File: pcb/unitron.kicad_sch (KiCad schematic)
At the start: 67 parts, among them J1 Conn_01x09_Female, J2 Conn_01x09_Male, J3 Conn_01x09_Female, J4 Conn_01x09_Male, J5 Conn_02x03_Odd_Even, Q1 FDN340P, Q2 BSS123, SW1 SW_SPST, U1 LTC-4727JS, U2 LTC-4727JS, U3 AS1115-BSST, U4 ATSAMD21E, U5 LTC-4727JR, U6 LTC-4727JR, U7 AS1115-BSST

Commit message: PCB v1.5
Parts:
- removed BT2: 2466, Battery:BatteryHolder_Keystone_2466_1xAAA, symbol Device:Battery
- removed D14: LED, LED_SMD:LED_0805_2012Metric, symbol Device:LED
- removed R2: 10KΩ, Resistor_SMD:R_0805_2012Metric, symbol Device:R_Small_US
- added S16: Gateron Blue, Button_Switch_Keyboard:SW_Cherry_MX_1.00u_PCB, symbol imperializer-rescue:switch_momentary_2pin-asl_symbols-imperializer-rescue
- added U8: AT24C01C-STUM, Package_TO_SOT_SMD:SOT-23-5, symbol asl_symbols_new:AT24C01C-STUM
- BT1: value 2466 -> 2468
- D1, D10, D11, D12, D2, D3, D4, D5, D6, D7, D8, D9: footprint LED_SMD:LED-APA102-2020 -> asl_footprints:LED-APA102-2020
- J1, J3: footprint Connector_PinSocket_2.54mm:PinSocket_1x09_P2.54mm_Vertical -> Connector_PinSocket_2.54mm:PinSocket_1x09_P2.54mm_Vertical_SMD_Pin1Left
- S4: footprint Button_Switch_Keyboard:SW_Cherry_MX_2.00u_PCB -> Button_Switch_Keyboard:SW_Cherry_MX_1.00u_PCB
- SW1: footprint asl_footprints:B12AP -> asl_footprints:switch_nkk_reinforced_pc_pin
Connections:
- net CKI: now also D6.4 (SDI), J3.8 (Pin_8); no longer D12.5 (CKI), J3.1 (Pin_1)
- net GND: now also BT1.2 (-), C2.2, J4.1 (Pin_1), U8.2 (GND), U8.5 (WP); no longer J4.3 (Pin_3)
- net GND_daughter: now also J3.1 (Pin_1); no longer J3.3 (Pin_3)
- net IRQ: now also J3.7 (Pin_7); no longer J3.9 (Pin_9)
- net IRQ_mcu: now also J4.7 (Pin_7); no longer J4.9 (Pin_9)
- net KEYA: now also J4.5 (Pin_5), S16.1; no longer J4.7 (Pin_7)
- net KEYB: now also J4.6 (Pin_6); no longer J4.8 (Pin_8)
- net MOSI: now also J4.9 (Pin_9); no longer J4.2 (Pin_2)
- net SCK: now also J4.8 (Pin_8); no longer J4.1 (Pin_1)
- net SCL: now also J3.3 (Pin_3); no longer J3.5 (Pin_5)
- net SCL_mcu: now also J4.3 (Pin_3), U8.1 (SCL); no longer J4.5 (Pin_5)
- net SDA: now also J3.4 (Pin_4); no longer J3.6 (Pin_6)
- net SDA_mcu: now also J4.4 (Pin_4), U8.3 (SDA); no longer J4.6 (Pin_6)
- net SDI: now also D6.5 (CKI), J3.9 (Pin_9); no longer D12.4 (SDI), J3.2 (Pin_2)
- net VIN: now also J4.2 (Pin_2), U8.4 (Vcc); no longer J4.4 (Pin_4)
- net VIN_daughter: now also J3.2 (Pin_2); no longer J3.4 (Pin_4)
- net at U3.11 (KEYA): now also J3.5 (Pin_5); no longer J3.7 (Pin_7)
- net at U3.12 (KEYB): now also J3.6 (Pin_6); no longer J3.8 (Pin_8)
- net at J2.7 (Pin_7), S12.2: now also S16.2
- net at D8.2 (CKO): now also D1.5 (CKI); no longer D2.5 (CKI)
- net at D8.3 (SDO): now also D1.4 (SDI); no longer D2.4 (SDI)
- net at D8.4 (SDI): now also D2.3 (SDO); no longer D3.3 (SDO)
- net at D8.5 (CKI): now also D2.2 (CKO); no longer D3.2 (CKO)
- net at D3.4 (SDI): now also D10.3 (SDO); no longer D9.3 (SDO)
- net at D3.5 (CKI): now also D10.2 (CKO); no longer D9.2 (CKO)
- net at D1.2 (CKO): now also D7.5 (CKI)
- net at D1.3 (SDO): now also D7.4 (SDI)
- net at D7.3 (SDO): no longer D1.4 (SDI)
- net at D7.2 (CKO): no longer D1.5 (CKI)
- net at D12.2 (CKO): now also D5.5 (CKI); no longer D6.5 (CKI)
- net at D12.3 (SDO): now also D5.4 (SDI); no longer D6.4 (SDI)
- net at D9.4 (SDI): now also D3.3 (SDO); no longer D4.3 (SDO)
- net at D9.5 (CKI): now also D3.2 (CKO); no longer D4.2 (CKO)
- net at D5.2 (CKO): now also D11.5 (CKI); no longer D10.5 (CKI)
- net at D5.3 (SDO): now also D11.4 (SDI); no longer D10.4 (SDI)
- net at D11.3 (SDO): now also D4.4 (SDI); no longer D5.4 (SDI)
- net at D11.2 (CKO): now also D4.5 (CKI); no longer D5.5 (CKI)
- net at D6.2 (CKO): now also D12.5 (CKI); no longer D11.5 (CKI)
- net at D6.3 (SDO): now also D12.4 (SDI); no longer D11.4 (SDI)
- net neopixel_mcu: no longer names the net of U4.11 (PA08(D4))
- new net: D2.4 (SDI), D9.3 (SDO)
- new net: D2.5 (CKI), D9.2 (CKO)
- new net: D10.5 (CKI), D4.2 (CKO)
- new net: D10.4 (SDI), D4.3 (SDO)
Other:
- moved on the sheet: BT1, D1, D10, D11, D12, D2, D3, D4, D5, D6, D7, D8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

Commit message: pcb v1.6
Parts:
- removed D1, D10, D11, D12, D2, D3, D4, D5, D6, D7, D8, D9: APA102-2020, asl_footprints:LED-APA102-2020, symbol LED:APA102-2020
- added D1, D10, D2, D3, D4, D5, D6, D7, D8, D9: SK9822, asl_footprints:LED_SK9822_5050, symbol asl_symbols_new:SK9822
- added R7, R8: 10KΩ, Resistor_SMD:R_0805_2012Metric, symbol Device:R_Small_US
- added U1: AP2112K-3.3, Package_TO_SOT_SMD:SOT-23-5, symbol asl_symbols_new:AP2112K-3.3
- BT1: footprint Battery:BatteryHolder_Keystone_2468_2xAAA -> Battery:BatteryHolder_Keystone_2479_3xAAA
- C2, C3: value 0.1µF -> 100nF
- J1, J3: value Conn_01x09_Female -> Conn_01x10_Male; footprint Connector_PinSocket_2.54mm:PinSocket_1x09_P2.54mm_Vertical_SMD_Pin1Left -> Connector_PinSocket_2.54mm:PinSocket_1x10_P2.54mm_Vertical_SMD_Pin1Right; symbol Connector:Conn_01x09_Female -> Connector:Conn_01x10_Male
- J2, J4: value Conn_01x09_Male -> Conn_01x10_Female; footprint Connector_PinHeader_2.54mm:PinHeader_1x09_P2.54mm_Vertical -> Connector_PinHeader_2.54mm:PinHeader_1x10_P2.54mm_Vertical; symbol Connector:Conn_01x09_Male -> Connector:Conn_01x10_Female
- renumbered D13 to D11, R9 to R10, R10 to R11, R11 to R12, R12 to R13, R13 to R14, R14 to R15, R3 to R2, R4 to R3, R5 to R4, R6 to R5, R7 to R6, R8 to R9, S9 to S10, S10 to S11, S11 to S12, S12 to S13, S13 to S14, S14 to S15, S15 to S16, S16 to S7, S7 to S8, S8 to S9, U1 to U2, U2 to U3, U3 to U4, U4 to U5, U8 to U6, U5 to U7, U6 to U8, U7 to U9
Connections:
- net CKI: now also D5.2 (CI)
- net GND: now also R8.2, U1.2 (GND)
- net GND_daughter: now also D1.3 (GND), D10.3 (GND), D2.3 (GND), D3.3 (GND), D4.3 (GND), D5.3 (GND), D6.3 (GND), D7.3 (GND), D8.3 (GND), D9.3 (GND)
- net SDI: now also D5.1 (DI)
- net VBATT: now also R7.1
- net VIN: now also U1.5 (VOUT); no longer Q1.3 (D)
- net VIN_daughter: now also D1.4 (VCC), D10.4 (VCC), D2.4 (VCC), D3.4 (VCC), D4.4 (VCC), D5.4 (VCC), D6.4 (VCC), D7.4 (VCC), D8.4 (VCC), D9.4 (VCC)
- net at J2.7 (Pin_7), S13.2: no longer S7.2
- net at J2.9 (Pin_9), S15.2: now also S7.2
- net batt_lvl: now reaches U5.6 (PA05(A4))
- net batt_lvl: now also R7.2, R8.1
- new net: Q1.3 (D), U1.1 (VIN), U1.3 (EN)
- new net: D10.6 (DO), D4.1 (DI)
- new net: D10.5 (CO), D4.2 (CI)
- new net: D4.5 (CO), D9.2 (CI)
- new net: D4.6 (DO), D9.1 (DI)
- new net: D2.6 (DO), D7.1 (DI)
- new net: D2.5 (CO), D7.2 (CI)
- new net: D1.2 (CI), D7.5 (CO)
- new net: D1.1 (DI), D7.6 (DO)
- new net: D1.6 (DO), D6.1 (DI)
- new net: D1.5 (CO), D6.2 (CI)
- new net: D3.1 (DI), D9.6 (DO)
- new net: D3.2 (CI), D9.5 (CO)
- new net: D3.5 (CO), D8.2 (CI)
- new net: D3.6 (DO), D8.1 (DI)
- new net: D2.2 (CI), D8.5 (CO)
- new net: D2.1 (DI), D8.6 (DO)
- new net: D10.2 (CI), D5.5 (CO)
- new net: D10.1 (DI), D5.6 (DO)
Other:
- moved on the sheet: BT1, C1, C2, C3, D11, H1, H2, H3, H4, J5, Q1, Q2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

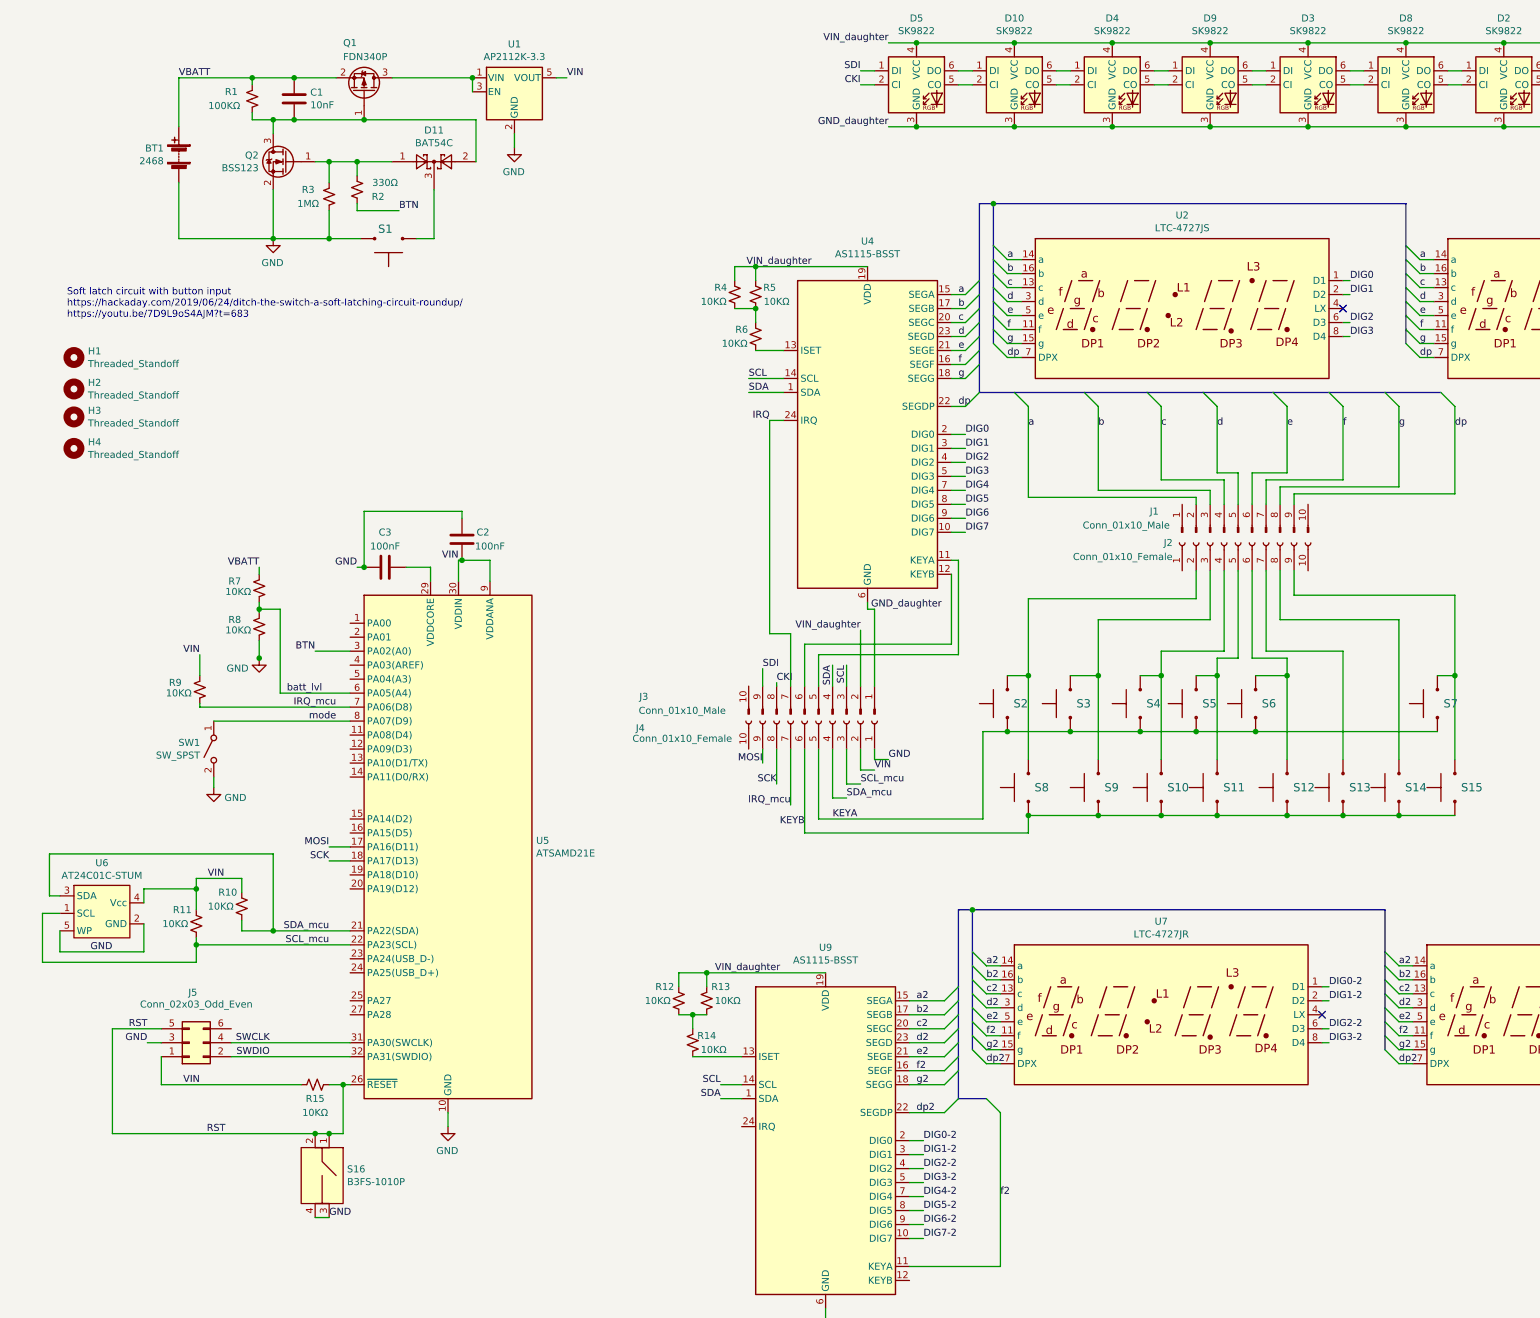
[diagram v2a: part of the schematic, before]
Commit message: unitron v 1.8
changed to QT PY and added lipo battery charging circuit
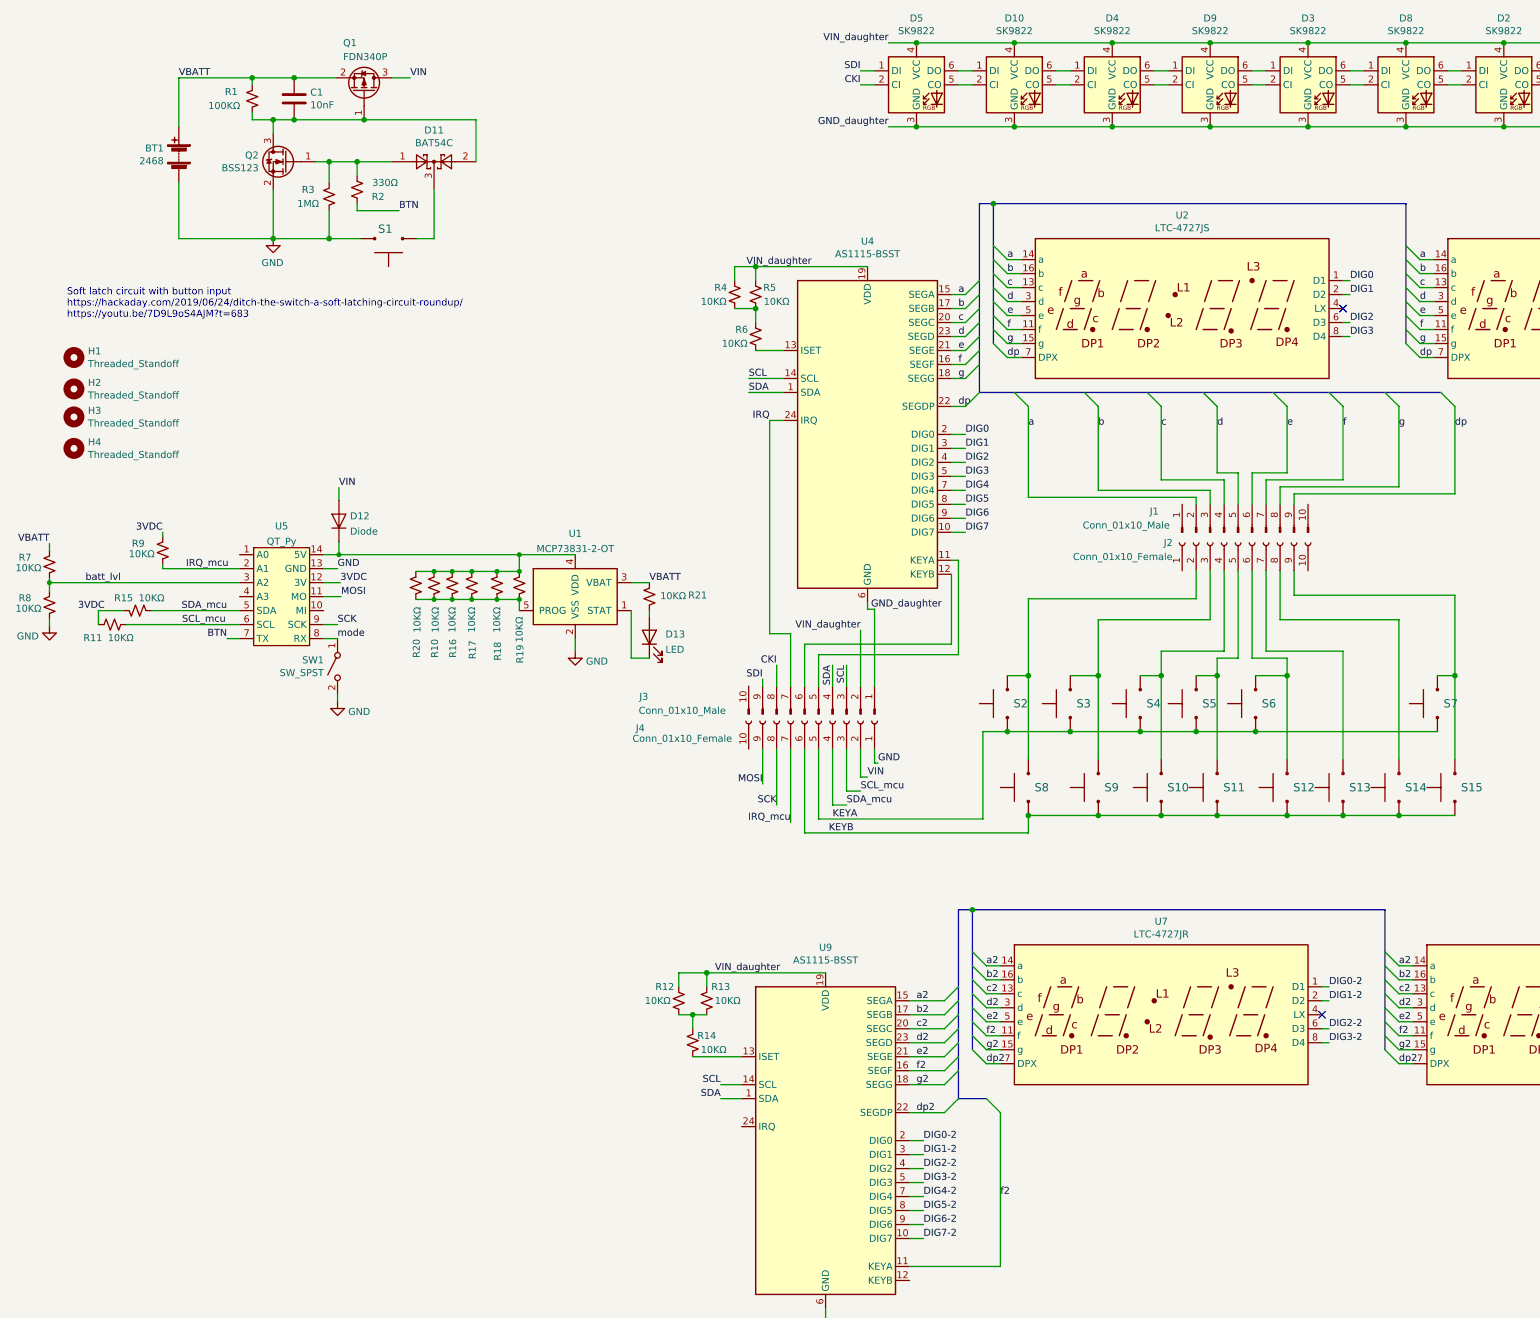
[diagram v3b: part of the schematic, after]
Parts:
- removed C2, C3: 100nF, Capacitor_SMD:C_0805_2012Metric, symbol Device:C
- removed J5: Conn_02x03_Odd_Even, asl_footprints:Tag-Connect_TC2030-IDC-NL_2x03_P1.27mm_Vertical, symbol Connector_Generic:Conn_02x03_Odd_Even
- removed S16: B3FS-1010P, asl_footprints:6mm_tactile_smd, symbol asl_symbols:B3FS-1010P
- removed U1: AP2112K-3.3, Package_TO_SOT_SMD:SOT-23-5, symbol asl_symbols_new:AP2112K-3.3
- removed U5: ATSAMD21E, Package_QFP:TQFP-32_7x7mm_P0.8mm, symbol asl_symbols_new:ATSAMD21E
- removed U6: AT24C01C-STUM, Package_TO_SOT_SMD:SOT-23-5, symbol asl_symbols_new:AT24C01C-STUM
- added D12: Diode, asl_footprints:D_SOD-123F, symbol asl_symbols_new:Diode
- added D13: LED, LED_SMD:LED_0805_2012Metric, symbol Device:LED
- added R16, R17, R18, R19, R20, R21: 10KΩ, Resistor_SMD:R_0805_2012Metric, symbol Device:R_Small_US
- added U1: MCP73831-2-OT, Package_TO_SOT_SMD:SOT-23-5, symbol Battery_Management:MCP73831-2-OT
- added U5: QT_Py, asl_footprints:QT_Py, symbol asl_symbols_new:QT_Py
- BT1: footprint Battery:BatteryHolder_Keystone_2479_3xAAA -> Connector_PinHeader_2.54mm:PinHeader_1x02_P2.54mm_Vertical
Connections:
- net RST is gone; now on net SDA_mcu: R15.1
- net BTN: now also U5.7 (TX)
- net GND: now also U1.2 (VSS), U5.13 (GND)
- net IRQ_mcu: now also U5.2 (A1)
- net MOSI: now also U5.11 (MO)
- net SCK: now also U5.9 (SCK)
- net SCL_mcu: now also U5.6 (SCL)
- net SDA_mcu: now also U5.5 (SDA); no longer R10.1
- net VBATT: now also R21.1, U1.3 (VBAT)
- net VIN: now also Q1.3 (D), D12.2 (A); no longer R10.2, R11.2, R15.2, R9.1
- net batt_lvl: now also U5.3 (A2)
- net mode: now also U5.8 (RX)
- new net: D12.1 (K), R10.1, R16.1, R17.1, R18.1, R19.1, R20.1, U1.4 (VDD), U5.14 (5V)
- new net: R10.2, R16.2, R17.2, R18.2, R19.2, R20.2, U1.5 (PROG)
- new net: D13.2 (A), R21.2
- new net: D13.1 (K), U1.1 (STAT)
- new net 3VDC: R11.2, R15.2, R9.1, U5.12 (3V)

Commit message: pcb v1.9
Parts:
- removed R10, R16, R17, R18, R20: 10KΩ, Resistor_SMD:R_0805_2012Metric, symbol Device:R_Small_US
- added R7, R8: 10KΩ, Resistor_SMD:R_0805_2012Metric, symbol Device:R_Small_US
- D1: renamed from D5; value SK9822 -> WS2812B; footprint asl_footprints:LED_SK9822_5050 -> LED_SMD:LED_WS2812B_PLCC4_5.0x5.0mm_P3.2mm; symbol asl_symbols_new:SK9822 -> LED:WS2812B
- D10: renamed from D6; value SK9822 -> WS2812B; footprint asl_footprints:LED_SK9822_5050 -> LED_SMD:LED_WS2812B_PLCC4_5.0x5.0mm_P3.2mm; symbol asl_symbols_new:SK9822 -> LED:WS2812B
- D2: renamed from D10; value SK9822 -> WS2812B; footprint asl_footprints:LED_SK9822_5050 -> LED_SMD:LED_WS2812B_PLCC4_5.0x5.0mm_P3.2mm; symbol asl_symbols_new:SK9822 -> LED:WS2812B
- D3: renamed from D4; value SK9822 -> WS2812B; footprint asl_footprints:LED_SK9822_5050 -> LED_SMD:LED_WS2812B_PLCC4_5.0x5.0mm_P3.2mm; symbol asl_symbols_new:SK9822 -> LED:WS2812B
- D4: renamed from D9; value SK9822 -> WS2812B; footprint asl_footprints:LED_SK9822_5050 -> LED_SMD:LED_WS2812B_PLCC4_5.0x5.0mm_P3.2mm; symbol asl_symbols_new:SK9822 -> LED:WS2812B
- D5: renamed from D3; value SK9822 -> WS2812B; footprint asl_footprints:LED_SK9822_5050 -> LED_SMD:LED_WS2812B_PLCC4_5.0x5.0mm_P3.2mm; symbol asl_symbols_new:SK9822 -> LED:WS2812B
- D6: renamed from D8; value SK9822 -> WS2812B; footprint asl_footprints:LED_SK9822_5050 -> LED_SMD:LED_WS2812B_PLCC4_5.0x5.0mm_P3.2mm; symbol asl_symbols_new:SK9822 -> LED:WS2812B
- D7: renamed from D2; value SK9822 -> WS2812B; footprint asl_footprints:LED_SK9822_5050 -> LED_SMD:LED_WS2812B_PLCC4_5.0x5.0mm_P3.2mm; symbol asl_symbols_new:SK9822 -> LED:WS2812B
- D8: renamed from D7; value SK9822 -> WS2812B; footprint asl_footprints:LED_SK9822_5050 -> LED_SMD:LED_WS2812B_PLCC4_5.0x5.0mm_P3.2mm; symbol asl_symbols_new:SK9822 -> LED:WS2812B
- D9: renamed from D1; value SK9822 -> WS2812B; footprint asl_footprints:LED_SK9822_5050 -> LED_SMD:LED_WS2812B_PLCC4_5.0x5.0mm_P3.2mm; symbol asl_symbols_new:SK9822 -> LED:WS2812B
- J1, J3: footprint Connector_PinSocket_2.54mm:PinSocket_1x10_P2.54mm_Vertical_SMD_Pin1Right -> Connector_PinSocket_2.54mm:PinSocket_1x08_P2.54mm_Vertical_SMD_Pin1Right; symbol Connector:Conn_01x10_Male -> Connector:Conn_01x08_Male
- J2, J4: footprint Connector_PinHeader_2.54mm:PinHeader_1x10_P2.54mm_Vertical -> Connector_PinHeader_2.54mm:PinHeader_1x08_P2.54mm_Vertical; symbol Connector:Conn_01x10_Female -> Connector:Conn_01x08_Female
- renumbered R7 to R10, R21 to R11, R8 to R12, R15 to R13, R11 to R14, R19 to R15, R12 to R16, R13 to R17, R14 to R18, U2 to U1, U3 to U2, U4 to U3, U5 to U4, U1 to U5, U7 to U6, U8 to U7, U9 to U8
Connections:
- net 3VDC: now also J4.2 (Pin_2)
- net GND: now also R15.1, R7.2
- net VBATT: no longer R11.1
- net VIN: no longer J4.2 (Pin_2)
- net VIN_daughter: now also D1.1 (VDD), D10.1 (VDD), D2.1 (VDD), D3.1 (VDD), D4.1 (VDD), D5.1 (VDD), D6.1 (VDD), D7.1 (VDD), D8.1 (VDD), D9.1 (VDD); no longer D1.4 (VCC), D10.4 (VCC), D2.4 (VCC), D3.4 (VCC), D4.4 (VCC), D5.4 (VCC), D6.4 (VCC), D7.4 (VCC), D8.4 (VCC), D9.4 (VCC)
- net a: now also J1.1 (Pin_1); no longer J1.2 (Pin_2)
- net b: now also J1.2 (Pin_2); no longer J1.3 (Pin_3)
- net c: now also J1.3 (Pin_3); no longer J1.4 (Pin_4)
- net d: now also J1.4 (Pin_4); no longer J1.5 (Pin_5)
- net dp: now also J1.8 (Pin_8); no longer J1.9 (Pin_9)
- net e: now also J1.5 (Pin_5); no longer J1.6 (Pin_6)
- net f: now also J1.6 (Pin_6); no longer J1.7 (Pin_7)
- net g: now also J1.7 (Pin_7); no longer J1.8 (Pin_8)
- net at S2.2, S8.2: now also J2.1 (Pin_1); no longer J2.2 (Pin_2)
- net at S3.2, S9.2: now also J2.2 (Pin_2); no longer J2.3 (Pin_3)
- net at S10.2, S4.2: now also J2.3 (Pin_3); no longer J2.4 (Pin_4)
- net at S11.2, S5.2: now also J2.4 (Pin_4); no longer J2.5 (Pin_5)
- net at S13.2: now also J2.6 (Pin_6); no longer J2.7 (Pin_7)
- net at S12.2, S6.2: now also J2.5 (Pin_5); no longer J2.6 (Pin_6)
- net at S15.2, S7.2: now also J2.8 (Pin_8); no longer J2.9 (Pin_9)
- net at S14.2: now also J2.7 (Pin_7); no longer J2.8 (Pin_8)
- net at D12.1 (K), U4.14 (5V), U5.4 (VDD): now also R11.1, R8.1; no longer R15.1
- net at D3.2 (DOUT): now also D4.4 (DIN); no longer D2.5 (CO)
- net at D4.2 (DOUT): now also D5.4 (DIN); no longer D3.5 (CO)
- net at D8.2 (DOUT): now also D9.4 (DIN); no longer D7.5 (CO)
- net at D9.2 (DOUT): now also D10.4 (DIN); no longer D8.5 (CO)
- net at D10.2 (DOUT): no longer D9.5 (CO)
- net at D5.2 (DOUT): now also D6.4 (DIN); no longer D4.5 (CO)
- net at D6.2 (DOUT): now also D7.4 (DIN); no longer D5.5 (CO)
- net at D7.2 (DOUT): now also D8.4 (DIN); no longer D6.5 (CO)
- net at D2.2 (DOUT): now also D3.4 (DIN); no longer D1.5 (CO)
- net at U4.1 (A0): now also R7.1, R8.2
- net CKI: no longer names the net of D1.2 (DOUT)
- net CKI: now also D2.4 (DIN); no longer J3.8 (Pin_8)
- net MOSI: no longer names the net of U4.11 (MO)
- net MOSI: no longer J4.9 (Pin_9)
- net SCK renamed neo_mcu
- removed net SDI: D1.1 (DI), J3.9 (Pin_9)
- new net neopixel: D1.4 (DIN), J3.8 (Pin_8)
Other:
- moved on the sheet: D13, R11, R15, U5
